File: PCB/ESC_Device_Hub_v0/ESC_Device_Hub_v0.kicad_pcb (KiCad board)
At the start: 2 copper layers, 50 x 90 mm, 138 parts, among them J1 Conn_01x04, J10 Conn_01x06, J11 Conn_01x02, J12 Conn_01x02, J13 Conn_01x02, J14 Conn_01x02, J15 Conn_01x02, J16 Conn_01x02, J17 Conn_01x02, J18 Conn_01x02, J19 Conn_01x05, J2 Conn_01x04, J20 Conn_01x01, J21 Conn_01x01, J22 Conn_01x02, J3 Conn_01x04, J4 Conn_01x04, J5 Conn_01x04, J6 Conn_01x04, J7 Conn_01x06, J8 Conn_01x06, J9 Conn_01x06, SW1 SW_Push, SW2 SW_Push, SW3 SW_Coded_SH-7050, SW4 SW_DIP_x02, U1 ISO1042BQDWVRQ1, U18 USB_Type-C, U2 MCP2562FD-H/MF, U3 IS25LP064D-JLLE, U4 STM32H563RGVx, U5 NJW1933F1-AT, U6 TLP293, U7 NJM2884U1-33, U8 XC8114AA01PR-G, U9 XC8114AA01PR-G, Y1 FC2012SN 32.768K-70NNA0KC0

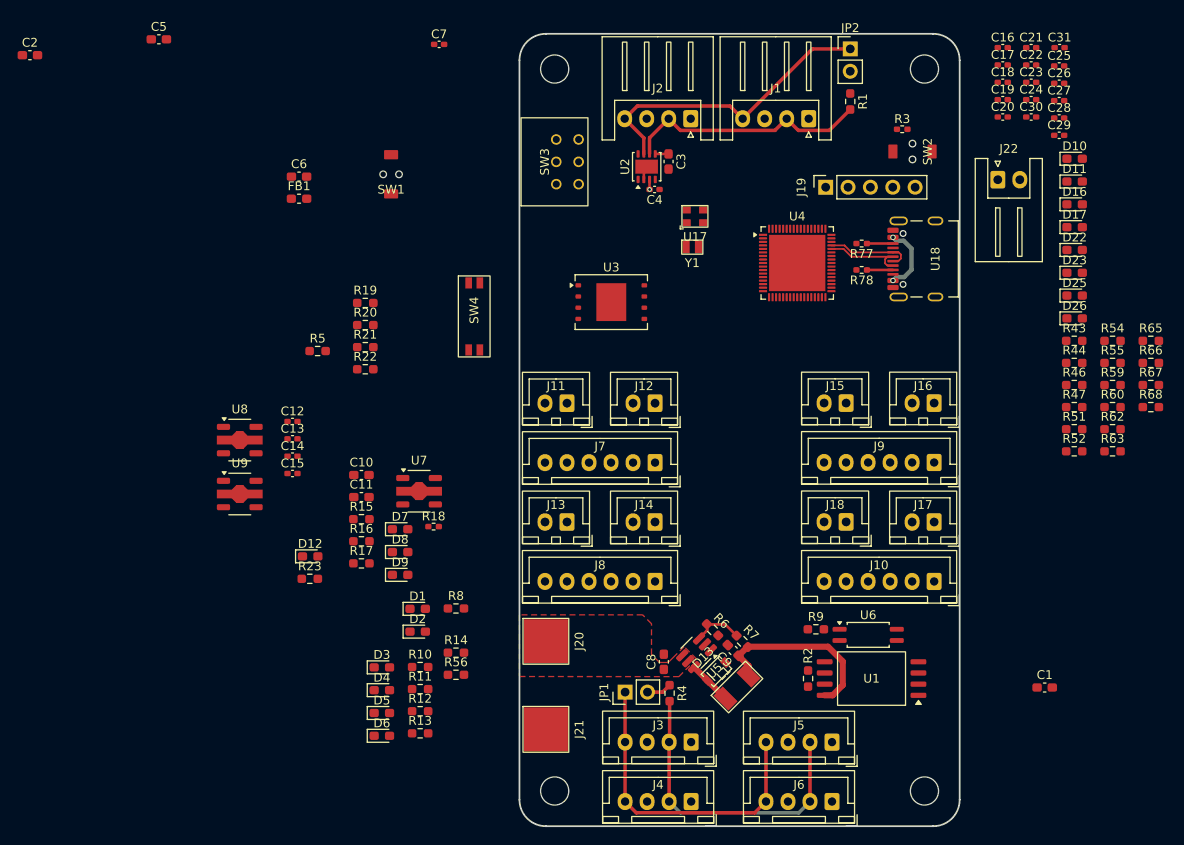
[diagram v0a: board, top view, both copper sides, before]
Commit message: PCB作成残りGNDのビア打ちをきちんとやるだけ
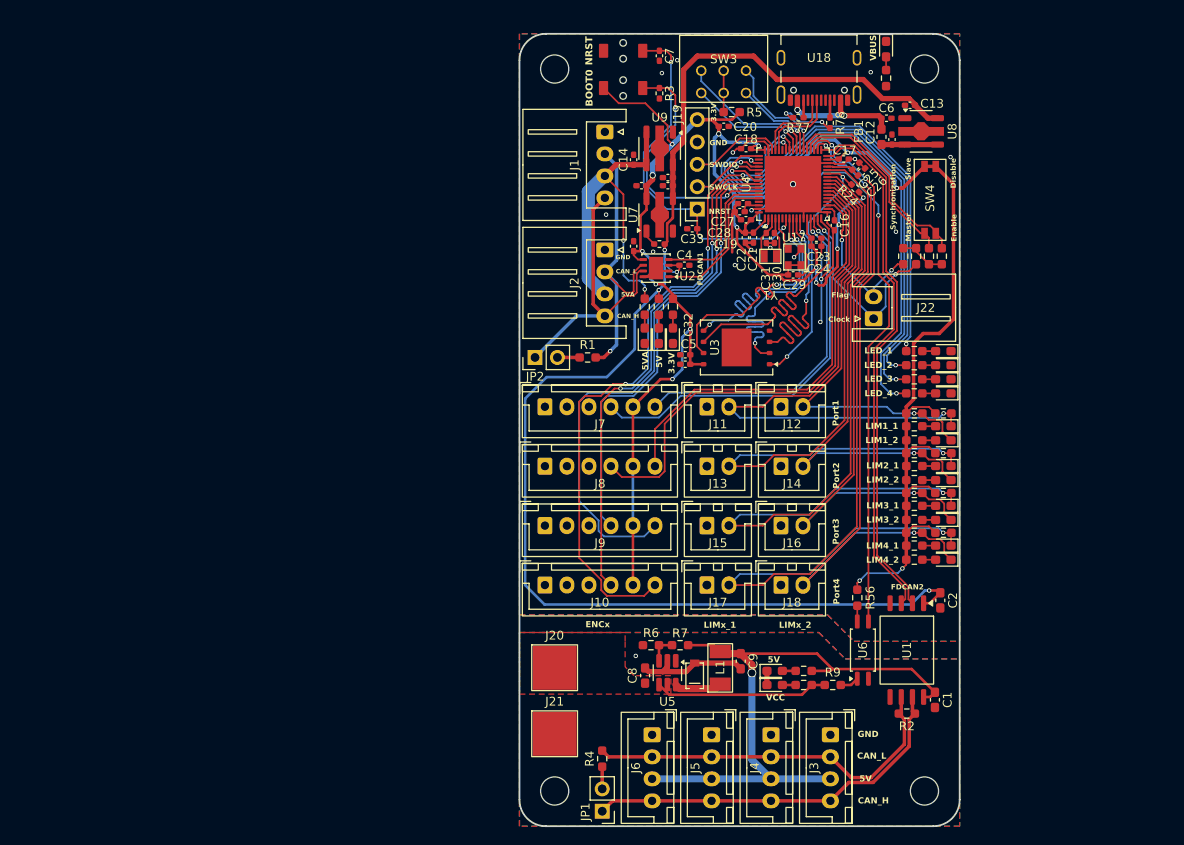
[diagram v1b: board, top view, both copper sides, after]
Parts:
- added C32: 1uF, Capacitor_SMD:C_0402_1005Metric_Pad0.74x0.62mm_HandSolder, F.Cu at (158.8, 66.5)
- added C33: 0.1uF, Capacitor_SMD:C_0402_1005Metric_Pad0.74x0.62mm_HandSolder, F.Cu at (159.6, 52.1)
- added R24: 10k, Resistor_SMD:R_0402_1005Metric_Pad0.72x0.64mm_HandSolder, F.Cu at (178.1, 47.5)
- C10, C11, C3, C5, C6: footprint Capacitor_SMD:C_0603_1608Metric_Pad1.08x0.95mm_HandSolder -> Capacitor_SMD:C_0402_1005Metric_Pad0.74x0.62mm_HandSolder
- C28: value 0.1uF -> 2.2uF
- U1: value ISO1042BQDWVRQ1 -> ISO1042BQDWVQ1
- moved C2 120.5 mm to (187.8, 94.3), turned to -90 degrees
- moved D12 87.2 mm to (181.6, 31.7), turned to -90 degrees
- moved R23 86.7 mm to (181.6, 35.0), turned to 90 degrees
- moved U8 85.0 mm to (185.6, 41.1)
- moved C13 79.7 mm to (184.4, 38.1), turned to 180 degrees
- moved C12 75.2 mm to (182.3, 42.0), turned to 90 degrees
- moved D6 74.7 mm to (188.1, 70.8), turned to 180 degrees
- moved D5 74.2 mm to (188.1, 69.2), turned to 180 degrees
- moved D4 73.7 mm to (188.1, 67.6), turned to 180 degrees
- moved D3 73.2 mm to (188.1, 66.0), turned to 180 degrees
- moved C5 70.3 mm to (158.8, 67.5), turned to 180 degrees
- moved R13 68.1 mm to (184.8, 70.8)
- moved R12 67.6 mm to (184.8, 69.2)
- moved R11 67.1 mm to (184.8, 67.6)
- moved C6 67.1 mm to (181.7, 39.6)
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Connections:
- C12 pad 1: Net-(U8-Vin) -> Net-(U8-EN)
- D23 pad 1: LIMS4_2 -> LIMS4_1
- D26 pad 1: LIMS4_1 -> LIMS4_2
- FB1 pad 2: Net-(U8-Vin) -> Net-(U8-EN)
- J17 pad 2: LIMS4_2 -> LIMS4_1
- J18 pad 2: LIMS4_1 -> LIMS4_2
- R60 pad 1: LIMS4_2 -> LIMS4_1
- R66 pad 1: LIMS4_1 -> LIMS4_2
- U4 pad 2: unconnected-(U4-PC13-Pad2) -> POWER_MONITOR
- U4 pad 26: POWER_MONITOR -> LIMS2_1
- U4 pad 27: LED_1 -> LIMS2_2
- U4 pad 28: LED_2 -> LIMS3_1
- U4 pad 30: unconnected-(U4-PB11-Pad30) -> LIMS3_2
- U4 pad 36: Rol_SW1 -> LIMS4_1
- U4 pad 37: Rol_SW2 -> LIMS4_2
- U4 pad 38: Rol_SW4 -> Synchronization_Master
- U4 pad 39: Rol_SW8 -> Synchronization_Enable
- U4 pad 40: LIMS2_1 -> Rol_SW1
- U4 pad 41: LIMS2_2 -> Rol_SW2
- U4 pad 42: LIMS3_1 -> Rol_SW4
- U4 pad 43: LIMS3_2 -> Rol_SW8
- U4 pad 54: LIMS4_2 -> LED_4
- U4 pad 55: LIMS4_1 -> LED_3
- U4 pad 56: unconnected-(U4-PC12-Pad56) -> LED_2
- U4 pad 57: LED_3 -> unconnected-(U4-PB3(JTDO-Pad57)
- U4 pad 58: LED_4 -> unconnected-(U4-PB4(NJTRST)-Pad58)
- U4 pad 59: unconnected-(U4-PB5-Pad59) -> LED_1
- U8 pad 2: Net-(U8-Vin) -> GND
- U8 pad 3: GND -> Net-(U8-EN)
- U8 pad 4: Net-(U8-Vin) -> Net-(U8-EN)
- U9 pad 2: +5VA -> GND
- U9 pad 3: GND -> +5VA
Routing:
- net +3.3V: track 1.51 -> 261.2 mm, vias 0 -> 18
- net +5V: track 1.14 -> 158.5 mm, vias 1 -> 4
- net LIMS4_1: track 0.00 -> 95.1 mm, vias 0 -> 3
- net GND: track 1.58 -> 85.2 mm, vias 0 -> 21
- net LIMS3_1: track 0.00 -> 81.7 mm, vias 0 -> 1
- net LIMS4_2: track 0.00 -> 80.1 mm, vias 0 -> 3
- net ENC4_A: track 0.00 -> 77.1 mm, vias 0 -> 4
- net LIMS2_1: track 0.00 -> 72.5 mm, vias 0 -> 1
- net POWER_MONITOR: track 0.00 -> 68.9 mm, vias 0 -> 2
- net LIMS3_2: track 0.00 -> 66.7 mm, vias 0 -> 1
- net ENC4_B: track 0.00 -> 65.4 mm, vias 0 -> 4
- net LIMS1_1: track 0.00 -> 64.0 mm, vias 0 -> 1
- net ENC3_A: track 0.00 -> 62.4 mm, vias 0 -> 1
- net ESC_FDCAN_TXD: track 0.00 -> 60.6 mm
- net ESC_FDCAN_RXD: track 0.00 -> 59.4 mm
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- added copper zone on B.Cu, net GND
- added copper zone on F.Cu, net GND
- added copper zone on B.Cu, net GNDD
- added copper zone on F.Cu, net GNDD
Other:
- board text added: "3.3V"
- board text added: "5V"
- board text added: "5VA"
- board text added: "BOOT0"
- board text added: "CAN_H"
- board text added: "CAN_L"
- board text added: "Clock"
- board text added: "Disable"
- board text added: "ENCx"
- board text added: "Enable"
- board text added: "FDCAN1"
- board text added: "FDCAN2"
- board text added: "Flag"
- board text added: "GND"
- board text added: "LED_1"
- board text added: "LED_2"
- board text added: "LED_3"
- board text added: "LED_4"
- board text added: "LIM1_1"
- board text added: "LIM1_2"
- board text added: "LIM2_1"
- board text added: "LIM2_2"
- board text added: "LIM3_1"
- board text added: "LIM3_2"
- board text added: "LIM4_1"
- board text added: "LIM4_2"
- board text added: "LIMx_1"
- board text added: "LIMx_2"
- board text added: "Master"
- board text added: "NRST"
- board text added: "Port1"
- board text added: "Port2"
- board text added: "Port3"
- board text added: "Port4"
- board text added: "SWCLK"
- board text added: "SWDIO"
- board text added: "Slave"
- board text added: "Synchronization"
- board text added: "VBUS"
- board text added: "VCC"
